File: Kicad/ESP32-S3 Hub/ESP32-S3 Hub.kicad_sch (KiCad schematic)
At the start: 26 parts, among them U1 ESP32-S3, Y1 ABM11-40.000MHZ-B1U-T3, 10ppm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

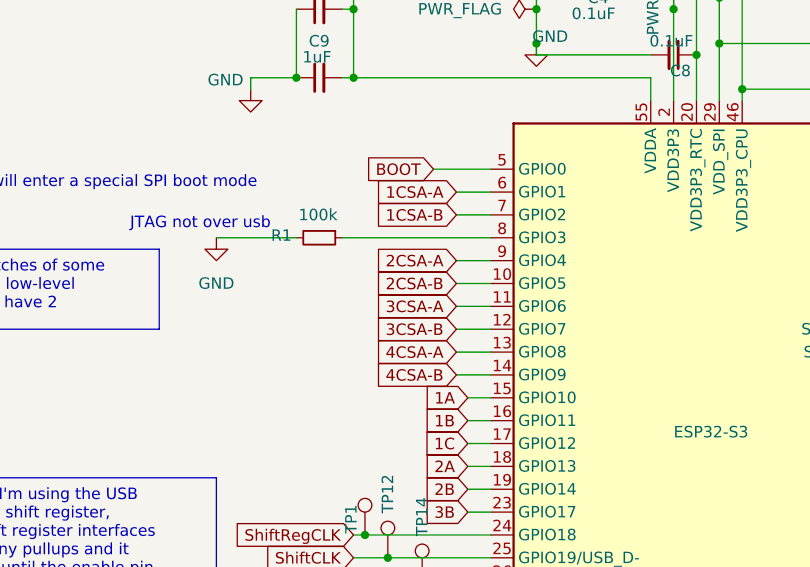
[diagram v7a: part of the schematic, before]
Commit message: Routed Current Sense lines
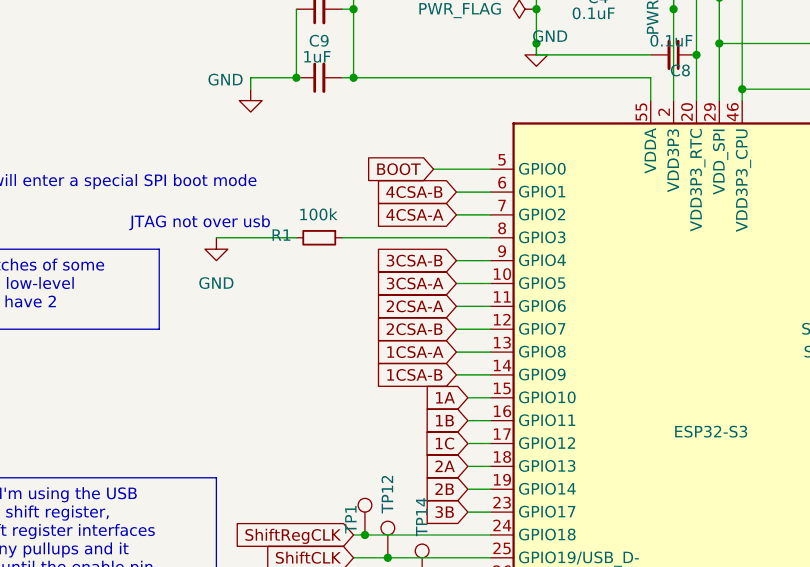
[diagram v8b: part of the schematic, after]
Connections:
- net 1CSA-A: now also U1.13 (GPIO8); no longer U1.6 (GPIO1)
- net 1CSA-B: now also U1.14 (GPIO9); no longer U1.7 (GPIO2)
- net 2CSA-A: now also U1.11 (GPIO6); no longer U1.9 (GPIO4)
- net 2CSA-B: now also U1.12 (GPIO7); no longer U1.10 (GPIO5)
- net 3CSA-A: now also U1.10 (GPIO5); no longer U1.11 (GPIO6)
- net 3CSA-B: now also U1.9 (GPIO4); no longer U1.12 (GPIO7)
- net 4CSA-A: now also U1.7 (GPIO2); no longer U1.13 (GPIO8)
- net 4CSA-B: now also U1.6 (GPIO1); no longer U1.14 (GPIO9)
